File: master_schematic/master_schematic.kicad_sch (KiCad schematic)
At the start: 10 parts, among them J1 Conn_01x02_Shielded, SW1 SW_SPST, U1 RFM95, U2 teensy_4.1, U3 EA50 Power Converter

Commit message: finding parts
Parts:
- added J21: Conn_01x02_Shielded, hb_footprint_lib:JST_S2B-PH-SM4-TB, symbol Connector_Generic:Conn_01x02
- added J22, J23: Conn_01x02_Shielded, symbol Connector_Generic_Shielded:Conn_01x02_Shielded
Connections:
- net +5V: now also J21.1 (Pin_1)
- net GND: now also J21.2 (Pin_2)
- no-connect marks 29 -> 35
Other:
- note added: "Note: these are external connectors and is not to be included on the board."

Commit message: edits after bom
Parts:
- J1: value Conn_01x02_Shielded -> 12V Female
- J21: value Conn_01x02_Shielded -> 5V Female
- J22: value Conn_01x02_Shielded -> 5V Male
- J23: value Conn_01x02_Shielded -> 12V Male
- SW1: footprint (none) -> hb_footprint_lib:SW_1201M2S3AQE2; Cost @ Qty (none) -> 14.68000; Manufacturer (none) -> C&K; Manufacturer Part # (none) -> 1201M2S3AQE2; Supplier (none) -> Digikey; Supplier Part # (none) -> CKN5054-ND; Unit Cost (none) -> 14.68000
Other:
- note added: "Note: we are buying a DPDT switch tho."
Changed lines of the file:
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@@
 		)
 	)
+	(text "Note: we are buying a DPDT switch tho."
+		(exclude_from_sim no)
+		(at 210.058 47.244 0)
+		(effects
+			(font
+				(size 1.27 1.27)
+			)
+		)
+	)
 	(label "PT4_I"
 		(at 134.62 166.37 0)
@@
 			)
 		)
-		(property "Value" "Conn_01x02_Shielded"
+		(property "Value" "5V Female"
 			(at 193.04 138.4299 0)
 			(effects
@@
 			)
 		)
-		(property "Footprint" ""
+		(property "Footprint" "hb_footprint_lib:SW_1201M2S3AQE2"
 			(at 187.96 52.07 0)
 			(effects
@@
 			)
 		)
-		(property "Datasheet" "~"
+		(property "Datasheet" "Datasheet"
+			(at 187.96 52.07 0)
+			(effects
+				(font
+					(size 1.27 1.27)
+				)
+				(hide yes)
+			)
+		)
+		(property "Description" "Slide Switch DPDT Through Hole, Right Angle"
+			(at 187.96 52.07 0)
+			(effects
+				(font
+					(size 1.27 1.27)
+				)
+				(hide yes)
+			)
+		)
+		(property "Manufacturer" "C&K"
+			(at 187.96 52.07 0)
+			(effects
+				(font
+					(size 1.27 1.27)
+				)
+				(hide yes)
+			)
+		)
+		(property "Manufacturer Part #" "1201M2S3AQE2"
+			(at 187.96 52.07 0)
+			(effects
+				(font
+					(size 1.27 1.27)
+				)
+				(hide yes)
+			)
+		)
+		(property "Supplier" "Digikey"
+			(at 187.96 52.07 0)
+			(effects
+				(font
+					(size 1.27 1.27)
+				)
+				(hide yes)
+			)
+		)
+		(property "Supplier Part #" "CKN5054-ND"
+			(at 187.96 52.07 0)
+			(effects
+				(font
+					(size 1.27 1.27)
+				)
+				(hide yes)
+			)
+		)
+		(property "Unit Cost" "14.68000"
 			(at 187.96 52.07 0)
 			(effects
@@
 			)
 		)
-		(property "Description" "Single Pole Single Throw (SPST) switch"
+		(property "Cost @ Qty" "14.68000"
 			(at 187.96 52.07 0)
 			(effects
@@
 			)
 		)
-		(property "Value" "Conn_01x02_Shielded"
+		(property "Value" "12V Male"
 			(at 208.28 149.8599 0)
 			(effects
@@
 			)
 		)
-		(property "Value" "Conn_01x02_Shielded"
+		(property "Value" "5V Male"
 			(at 242.57 149.8599 0)
 			(effects
@@
 			)
 		)
-		(property "Value" "Conn_01x02_Shielded"
+		(property "Value" "12V Female"
 			(at 193.04 113.0299 0)
 			(effects

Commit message: routed some annoying ass traces
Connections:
- net +3V3: now also U1.1 (VDD)
- net +5V: no longer U1.1 (VDD)
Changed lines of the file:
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@@
 		)
 	)
-	(label "+5V"
+	(label "+3V3"
 		(at 54.61 39.37 180)
 		(fields_autoplaced yes)
@@
 		)
 		(instances
-			(project ""
+			(project "master_schematic"
 				(path "/c4f7e98c-e88d-49cc-9841-b70710a90a72"
 					(reference "J22")

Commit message: FINALLY FINISHED ThESE DAMN TRACES F&#%%%
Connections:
- net MBV1-I-1: now also U2.28 (RX7); no longer U2.25 (A11)
- net MBV1-I-2: now also U2.29 (TX7); no longer U2.26 (A12)
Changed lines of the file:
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@@
-	)
-	(no_connect
-		(at 87.63 152.4)
 	)
 	(no_connect
@@
 	)
 	(no_connect
+		(at 87.63 121.92)
+	)
+	(no_connect
 		(at 78.74 41.91)
 	)
@@
 	)
 	(no_connect
+		(at 87.63 124.46)
+	)
+	(no_connect
+		(at 87.63 147.32)
+	)
+	(no_connect
 		(at 234.95 147.32)
 	)
 	(no_connect
-		(at 87.63 147.32)
-	)
-	(no_connect
 		(at 87.63 144.78)
 	)
@@
 	(no_connect
 		(at 200.66 147.32)
-	)
-	(no_connect
-		(at 87.63 149.86)
 	)
 	(no_connect
@@
 	)
 	(bus_entry
-		(at 67.31 119.38)
+		(at 67.31 147.32)
 		(size 2.54 2.54)
 		(stroke
@@
 	)
 	(bus_entry
-		(at 67.31 121.92)
+		(at 67.31 149.86)
 		(size 2.54 2.54)
 		(stroke
@@
 	(wire
 		(pts
-			(xy 69.85 124.46) (xy 87.63 124.46)
+			(xy 69.85 152.4) (xy 87.63 152.4)
 		)
 		(stroke
@@
 	(wire
 		(pts
-			(xy 69.85 121.92) (xy 87.63 121.92)
+			(xy 69.85 149.86) (xy 87.63 149.86)
 		)
 		(stroke
@@
 	(bus
 		(pts
-			(xy 67.31 119.38) (xy 67.31 121.92)
+			(xy 67.31 147.32) (xy 67.31 149.86)
 		)
 		(stroke
@@
 		)
 	)
-	(bus
-		(pts
-			(xy 67.31 116.84) (xy 67.31 119.38)
-		)
-		(stroke
-			(width 0)
-			(type default)
-		)
-	)
 	(wire
 		(pts
@@
 	(bus
 		(pts
+			(xy 67.31 144.78) (xy 52.07 144.78)
+		)
+		(stroke
+			(width 0)
+			(type default)
+		)
+	)
+	(bus
+		(pts
 			(xy 67.31 167.64) (xy 67.31 165.1)
 		)
@@
 		(pts
 			(xy 182.88 110.49) (xy 185.42 110.49)
+		)
+		(stroke
+			(width 0)
+			(type default)
+		)
+	)
+	(bus
+		(pts
+			(xy 67.31 144.78) (xy 67.31 147.32)
 		)
 		(stroke
@@
 	)
 	(label "MBV1-I-2"
-		(at 76.2 124.46 0)
+		(at 76.2 152.4 0)
 		(fields_autoplaced yes)
 		(effects
@@
 	)
 	(label "MBV1-I-1"
-		(at 76.2 121.92 0)
-		(fields_autoplaced yes)
-		(effects
-			(font
-				(size 1.27 1.27)
-			)
-			(justify left bottom)
-		)
-	)
+		(at 76.2 149.86 0)
+		(fields_autoplaced yes)
+		(effects
+			(font
+				(size 1.27 1.27)
+			)
+			(justify left bottom)
+		)
+	)
+	(label "{PV}"
+		(at 52.07 144.78 180)
+		(fields_autoplaced yes)
+		(effects
+			(font
+				(size 1.27 1.27)
+			)
+			(justify right bottom)
+		)
+	)

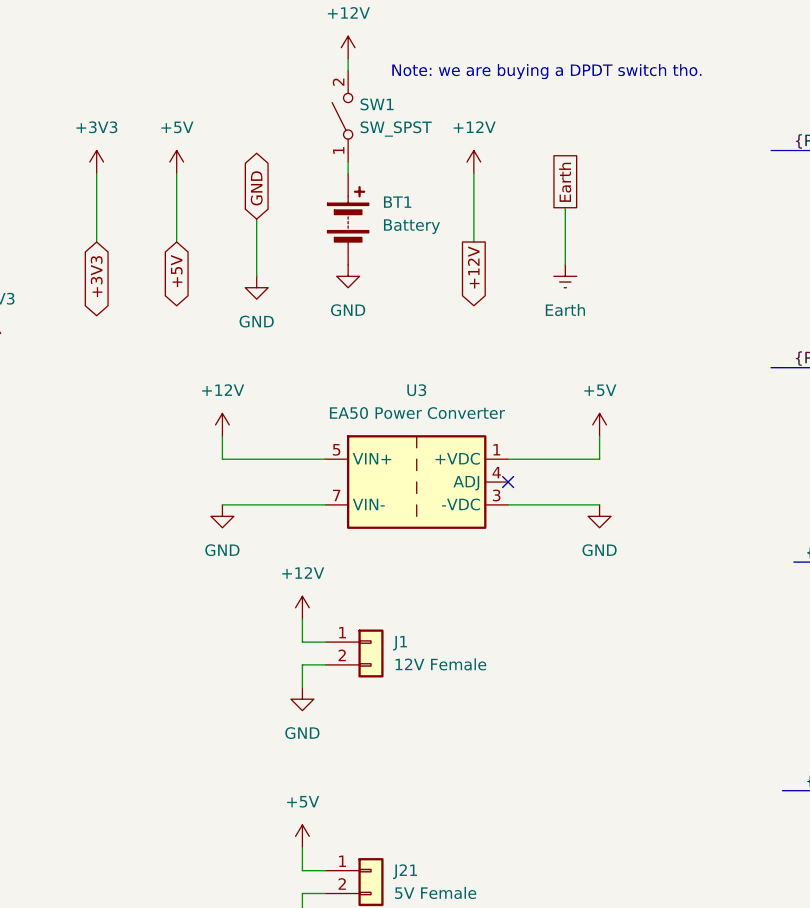
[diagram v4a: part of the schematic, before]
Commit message: Edited the switch to be in series with the circuit (instead of parallel)
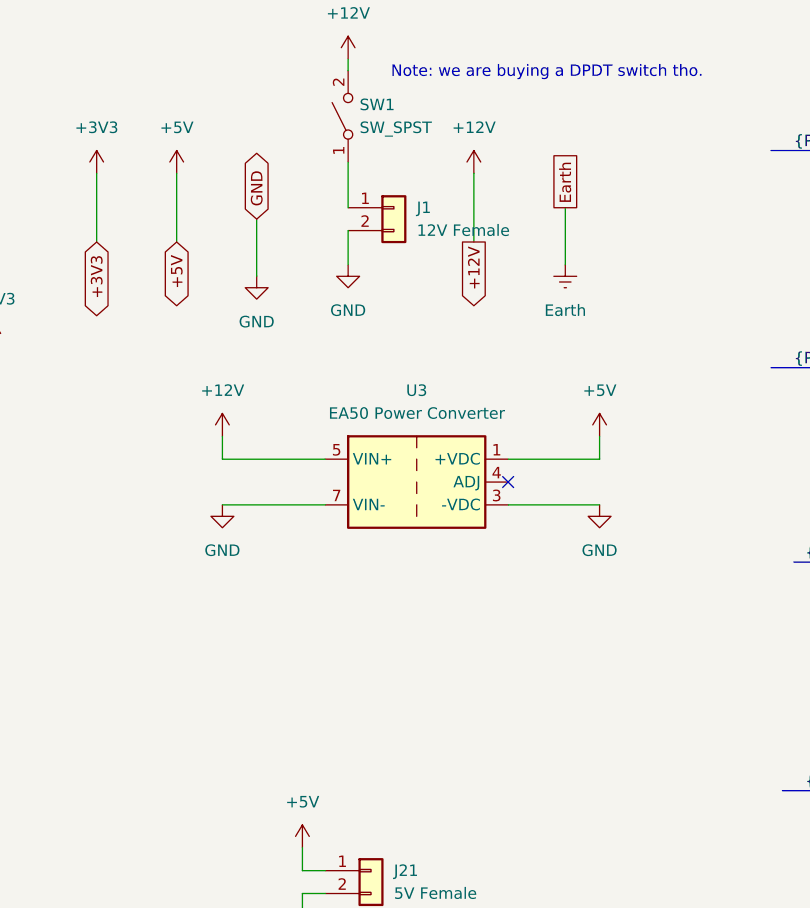
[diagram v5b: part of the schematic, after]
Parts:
- removed BT1: Battery, symbol Device:Battery
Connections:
- net +12V: no longer J1.1 (Pin_1)
- net at SW1.1 (A): now also J1.1 (Pin_1)
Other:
- moved on the sheet: J1

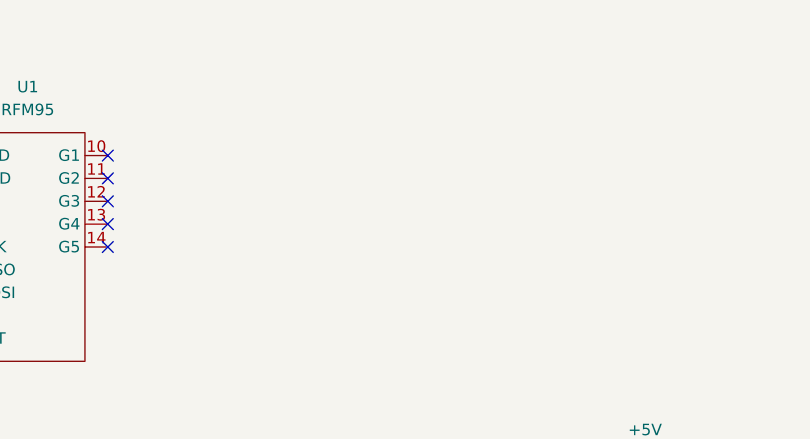
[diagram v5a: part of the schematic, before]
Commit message: Edited silkscreens
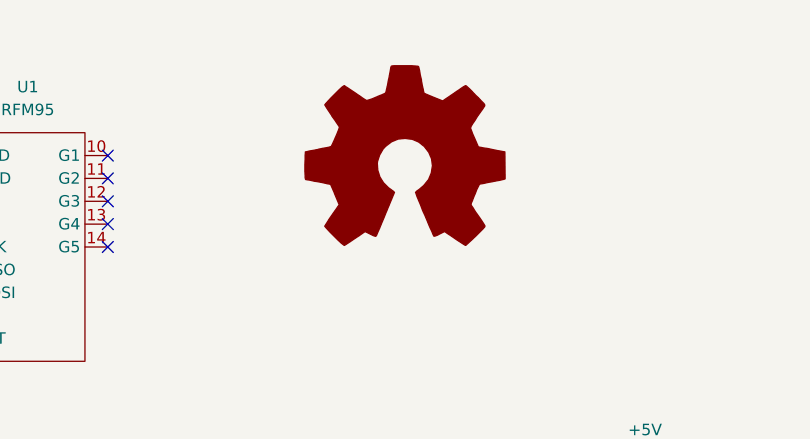
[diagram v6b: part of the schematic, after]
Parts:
- added SYM1: Logo_Open_Hardware_Large, hb_footprint_lib:ssilogo, symbol Graphic:Logo_Open_Hardware_Large
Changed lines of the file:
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@@
+	)
+	(symbol
+		(lib_id "Graphic:Logo_Open_Hardware_Large")
+		(at 111.76 40.64 0)
+		(unit 1)
+		(exclude_from_sim no)
+		(in_bom no)
+		(on_board yes)
+		(dnp no)
+		(fields_autoplaced yes)
+		(property "Reference" "SYM1"
+			(at 111.76 27.94 0)
+			(effects
+				(font
+					(size 1.27 1.27)
+				)
+				(hide yes)
+			)
+		)
+		(property "Value" "Logo_Open_Hardware_Large"
+			(at 111.76 50.8 0)
+			(effects
+				(font
+					(size 1.27 1.27)
+				)
+				(hide yes)
+			)
+		)
+		(property "Footprint" "hb_footprint_lib:ssilogo"
+			(at 111.76 40.64 0)
+			(effects
+				(font
+					(size 1.27 1.27)
+				)
+				(hide yes)
+			)
+		)
+		(property "Datasheet" "~"
+			(at 111.76 40.64 0)
+			(effects
+				(font
+					(size 1.27 1.27)
+				)
+				(hide yes)
+			)
+		)
+		(property "Description" "Open Hardware logo, large"
+			(at 111.76 40.64 0)
+			(effects
+				(font
+					(size 1.27 1.27)
+				)
+				(hide yes)
+			)
+		)
+		(property "Sim.Enable" "0"
+			(at 111.76 40.64 0)
+			(effects
+				(font
+					(size 1.27 1.27)
+				)
+				(hide yes)
+			)
+		)
+		(property "Manufacturer" ""
+			(at 111.76 40.64 0)
+			(effects
+				(font
+					(size 1.27 1.27)
+				)
+				(hide yes)
+			)
+		)
+		(property "Manufacturer Part #" ""
+			(at 111.76 40.64 0)
+			(effects
+				(font
+					(size 1.27 1.27)
+				)
+				(hide yes)
+			)
+		)
+		(property "Supplier" ""
+			(at 111.76 40.64 0)
+			(effects
+				(font
+					(size 1.27 1.27)
+				)
+				(hide yes)
+			)
+		)
+		(property "Supplier Part #" ""
+			(at 111.76 40.64 0)
+			(effects
+				(font
+					(size 1.27 1.27)
+				)
+				(hide yes)
+			)
+		)
+		(property "Unit Cost" ""
+			(at 111.76 40.64 0)
+			(effects
+				(font
+					(size 1.27 1.27)
+				)
+				(hide yes)
+			)
+		)
+		(property "Cost @ Qty" ""
+			(at 111.76 40.64 0)
+			(effects
+				(font
+					(size 1.27 1.27)
+				)
+				(hide yes)
+			)
+		)
+		(instances
+			(project "master_schematic"
+				(path "/c4f7e98c-e88d-49cc-9841-b70710a90a72"
+					(reference "SYM1")
+					(unit 1)
+				)
+			)
+		)
 	)
 	(symbol
